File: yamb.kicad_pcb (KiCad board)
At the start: 2 copper layers, 68.7 x 110.2 mm, 18 parts, among them J1 Barrel_Jack, J2 I2C, J4 HEADER_2.54, J5 Remote_Reset, J6 Power_Switch, P1 USB_C_Plug_USB2.0, SW1 RESET, U1 TPS3808DBV, U2 MCSBC, U3 SVR, U4 RAK4630, U5 BME280

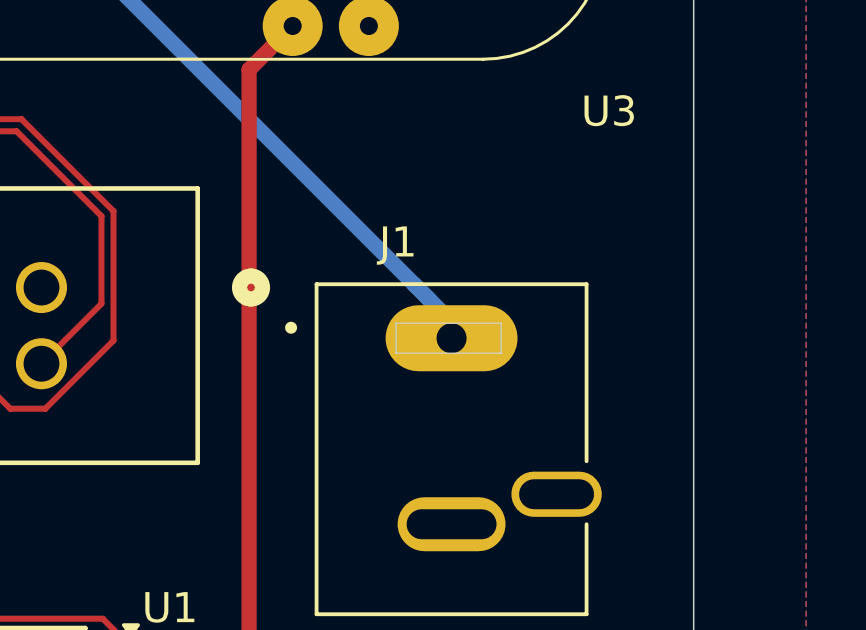
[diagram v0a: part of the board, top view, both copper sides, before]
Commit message: repaired J1 footprint edge cut issue
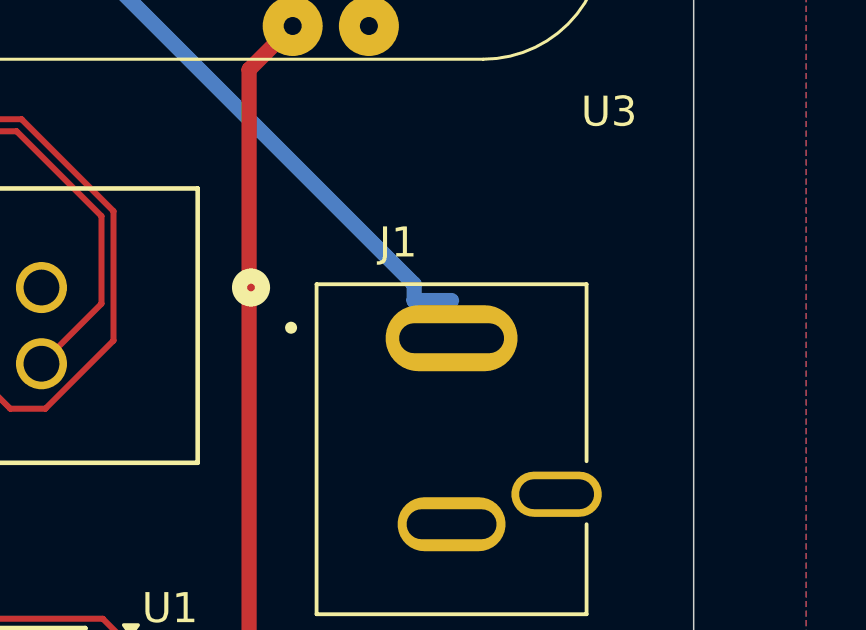
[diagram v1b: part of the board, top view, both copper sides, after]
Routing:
- net 7-20V: track 36.2 -> 35.4 mm
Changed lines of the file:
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@@
 		)
 		(fp_line
-			(start -1.85 -4.2)
-			(end 1.65 -4.2)
-			(stroke
-				(width 0.01)
-				(type solid)
-			)
-			(layer "Edge.Cuts")
-		)
-		(fp_line
-			(start -1.85 -3.2)
-			(end -1.85 -4.2)
-			(stroke
-				(width 0.01)
-				(type solid)
-			)
-			(layer "Edge.Cuts")
-		)
-		(fp_line
-			(start 1.65 -4.2)
-			(end 1.65 -3.2)
-			(stroke
-				(width 0.01)
-				(type solid)
-			)
-			(layer "Edge.Cuts")
-		)
-		(fp_line
-			(start 1.65 -3.2)
-			(end -1.85 -3.2)
-			(stroke
-				(width 0.01)
-				(type solid)
-			)
-			(layer "Edge.Cuts")
-		)
-		(fp_line
 			(start -4.75 -5.75)
 			(end 4.75 -5.75)
@@
 			(at 0 -3.7)
 			(size 4.4 2.2)
-			(drill 1)
+			(drill oval 3.5 1)
 			(layers "*.Cu" "*.Mask")
 			(remove_unused_layers no)
@@
 	)
 	(segment
-		(start 166.462465 89.312465)
-		(end 166 88.85)
+		(start 166 88.85)
+		(end 150.192 73.042)
 		(width 0.508)
 		(layer "B.Cu")
@@
 	)
 	(segment
-		(start 167.25 90.1)
-		(end 166 88.85)
-		(width 0.508)
-		(layer "B.Cu")
-		(net 14)
-	)
-	(segment
-		(start 166 88.85)
-		(end 150.192 73.042)
+		(start 166 89.395)
+		(end 167.25 89.395)
 		(width 0.508)
 		(layer "B.Cu")
@@
 	)
 	(segment
-		(start 166.545 89.395)
-		(end 166.462465 89.312465)
+		(start 166 88.85)
+		(end 166 89.395)
 		(width 0.508)
 		(layer "B.Cu")
@@
 		)
 	)
-	(generated
-		(type tuning_pattern)
-		(name "Tuning Pattern")
-		(layer "B.Cu")
-		(base_line
-			(pts
-				(xy 166.545 89.395) (xy 166.462465 89.312465)
-			)
-		)
-		(corner_radius_percent 80)
-		(end
-			(xy 166.462465 89.312465)
-		)
-		(initial_side "right")
-		(last_diff_pair_gap 0.18)
-		(last_netname "7-20V")
-		(last_status "tuned")
-		(last_track_width 0.508)
-		(last_tuning "29.9086 mm (tuned)")
-		(max_amplitude 1)
-		(min_amplitude 0.2)
-		(min_spacing 0.6)
-		(origin
-			(xy 166.545 89.395)
-		)
-		(override_custom_rules no)
-		(rounded yes)
-		(single_sided no)
-		(target_length 1000000)
-		(target_length_max 1000000)
-		(target_length_min 0)
-		(target_skew 0)
-		(target_skew_max 0.1)
-		(target_skew_min -0.1)
-		(tuning_mode "single")
-		(members "e272b570-c039-4ab2-b8a6-abd5d11b50f3")
-	)
 	(embedded_fonts no)
